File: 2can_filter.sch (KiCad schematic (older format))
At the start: 24 parts, among them J3 USB mini-B SMD, J4 NOT_FITTED_SWD_Conn_01x04_Male, U5 STM32F105RBTx, U6 TJA1040T, U7 TJA1040T, Y1 Crystal KX-13 25MHz

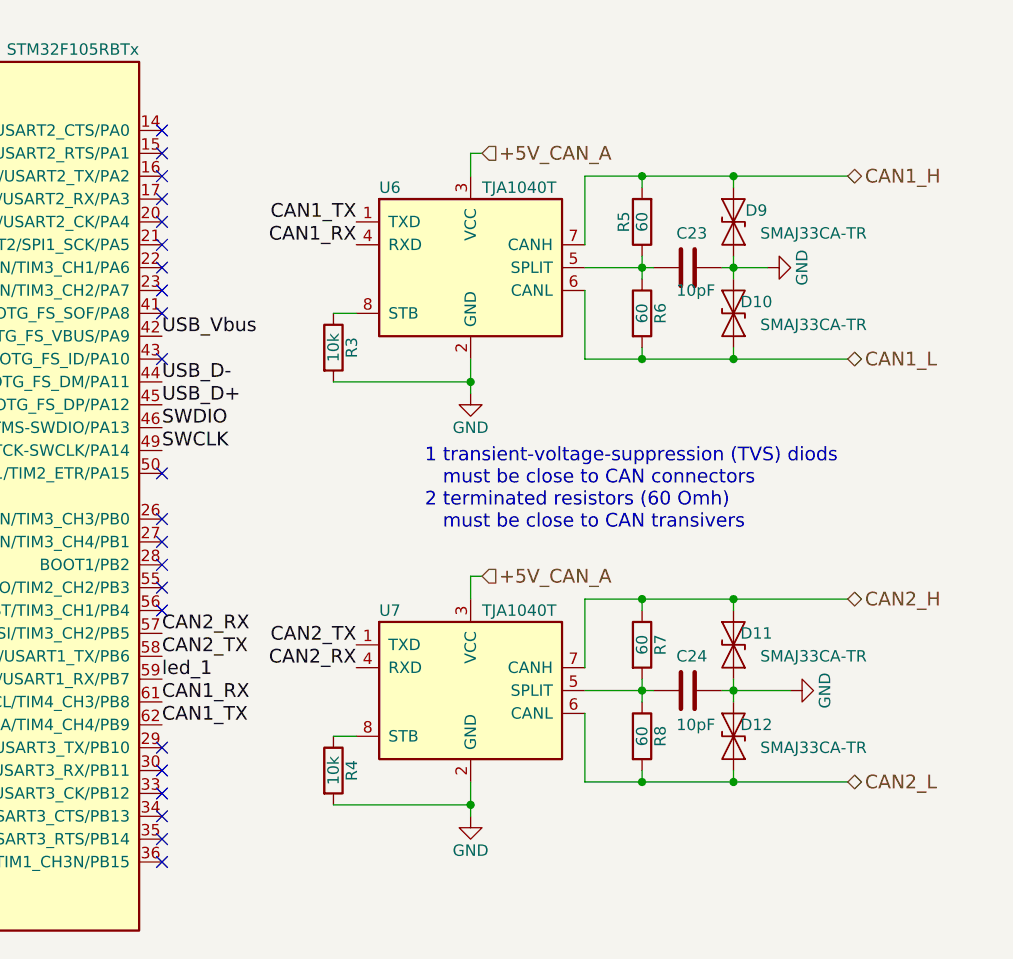
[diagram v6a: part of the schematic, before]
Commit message: fix CAN, swapped the stm->to->can connection in module B
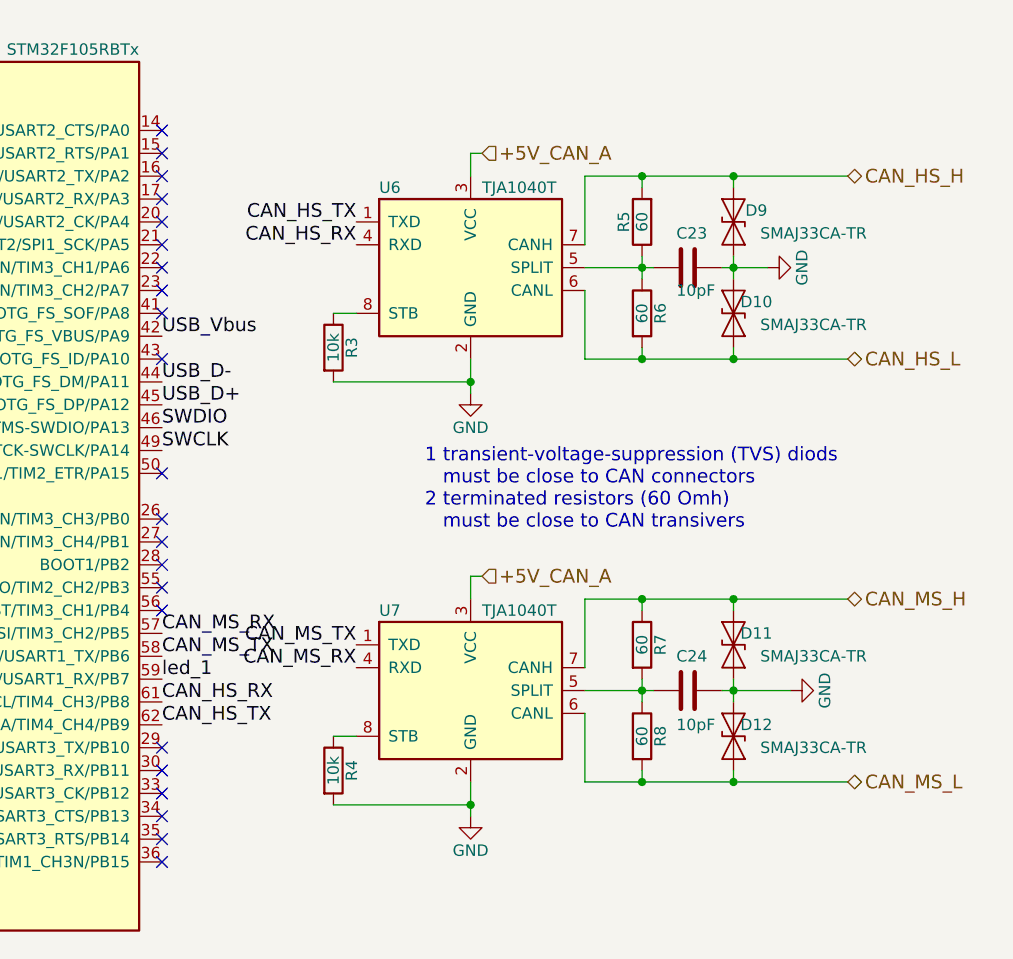
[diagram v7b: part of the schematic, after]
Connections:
- net CAN1_H renamed CAN_HS_H
- net CAN1_L renamed CAN_HS_L
- net CAN1_RX renamed CAN_HS_RX
- net CAN1_TX renamed CAN_HS_TX
- net CAN2_H renamed CAN_MS_H
- net CAN2_L renamed CAN_MS_L
- net CAN2_RX renamed CAN_MS_RX
- net CAN2_TX renamed CAN_MS_TX
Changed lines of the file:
@@
 LIBS:valves
 LIBS:stm32
-LIBS:LM2596SX-5.0_NOPB
-LIBS:lm2575s-5
-LIBS:74HC4050D
-LIBS:54819-0572
+LIBS:zpkl
 LIBS:instrument_cluster-cache
 EELAYER 25 0
@@
 +3V3_STM_A
 Text HLabel 10700 1500 2    60   BiDi ~ 0
-CAN1_H
+CAN_HS_H
 Text HLabel 10700 2300 2    60   BiDi ~ 0
-CAN1_L
+CAN_HS_L
 Text HLabel 10700 3350 2    60   BiDi ~ 0
-CAN2_H
+CAN_MS_H
 Text HLabel 10700 4150 2    60   BiDi ~ 0
-CAN2_L
+CAN_MS_L
 $Comp
 L TJA1040T U7
@@
 USB_Vbus
 Text Label 7700 3800 0    60   ~ 0
-CAN1_RX
+CAN_HS_RX
 Text Label 7700 3900 0    60   ~ 0
-CAN1_TX
+CAN_HS_TX
 Text Label 7700 3600 0    60   ~ 0
-CAN2_TX
+CAN_MS_TX
 Text Label 7700 3500 0    60   ~ 0
-CAN2_RX
+CAN_MS_RX
 Text Label 8550 3650 2    60   ~ 0
-CAN2_RX
+CAN_MS_RX
 Text Label 8550 3550 2    60   ~ 0
-CAN2_TX
+CAN_MS_TX
 Text Label 8550 1800 2    60   ~ 0
-CAN1_RX
+CAN_HS_RX
 Text Label 8550 1700 2    60   ~ 0
-CAN1_TX
+CAN_HS_TX
 $Comp
 L D_TVS D10

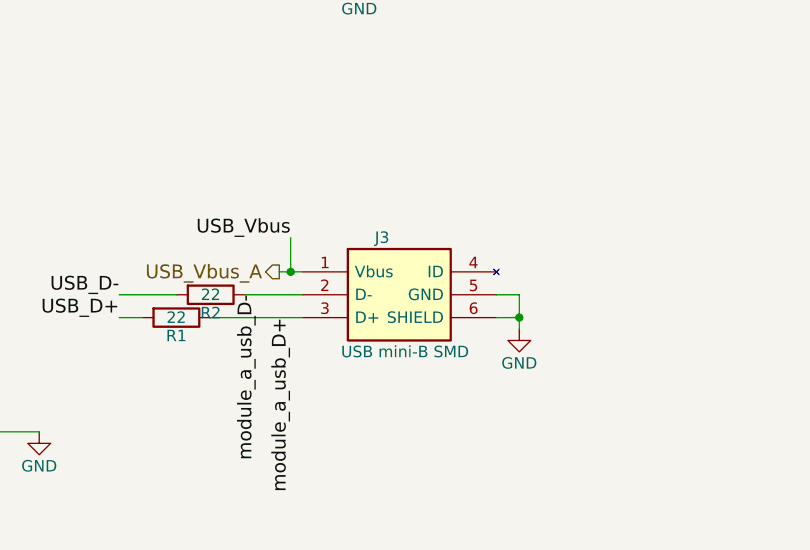
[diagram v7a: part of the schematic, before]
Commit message: fix USB footprint
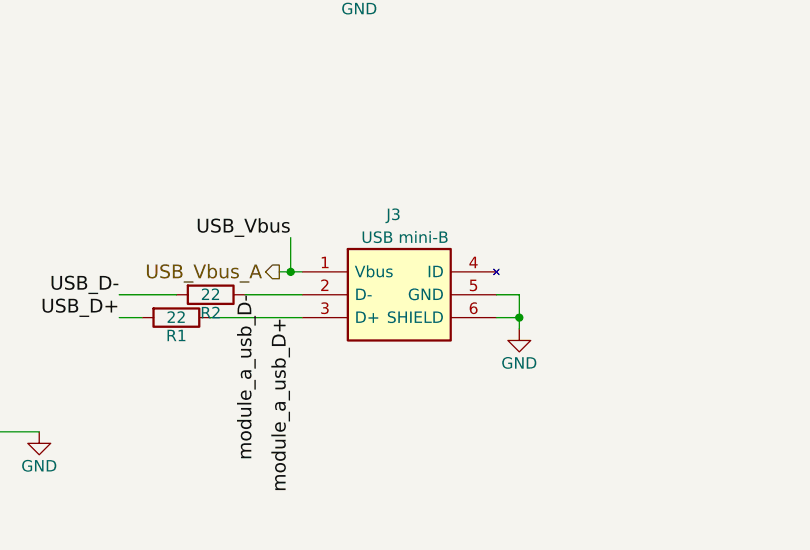
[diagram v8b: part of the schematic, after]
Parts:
- J3: value USB mini-B SMD -> USB mini-B; footprint zpkl:USB_mini_B -> zpkl:USB-B-M5-SMD-C
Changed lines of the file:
@@
 U 1 1 5A09A3F6
 P 4650 6400
-F 0 "J3" H 5000 6550 50  0000 C CNN
-F 1 "USB mini-B SMD" H 5100 6050 50  0000 C CNN
-F 2 "zpkl:USB_mini_B" H 5000 5950 50  0001 C CNN
+F 0 "J3" H 5050 6650 50  0000 C CNN
+F 1 "USB mini-B" H 5100 6550 50  0000 C CNN
+F 2 "zpkl:USB-B-M5-SMD-C" H 5000 5950 50  0001 C CNN
 F 3 "http://www.molex.com/webdocs/datasheets/pdf/en-us/0548190572_IO_CONNECTORS.pdf" H 5000 5850 50  0001 C CNN
 F 4 "Surface mount onthego connector,1A 30V Molex On-The-Go Series Right Angle SMT Version 2.0 Type B Mini USB Connector Receptacle, 30 V, 1A" H 5000 5750 50  0001 C CNN "Description"
